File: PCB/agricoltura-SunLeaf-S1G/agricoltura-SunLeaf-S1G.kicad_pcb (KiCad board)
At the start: 4 copper layers, 100 x 40 mm, 125 parts, among them M1 SPSGRF-915, Q1 DMP3125L-7, Q2 DMP3125L-7, SW1 B3U-1000P, T1 BM04B-SRSS-TB(LF)(SN), T10 BM04B-SRSS-TB(LF)(SN), T11 BM04B-SRSS-TB(LF)(SN), T12 BM04B-SRSS-TB(LF)(SN), T13 BM04B-SRSS-TB(LF)(SN), T14 BM04B-SRSS-TB(LF)(SN), T15 BM04B-SRSS-TB(LF)(SN), T16 BM04B-SRSS-TB(LF)(SN), T17 BM04B-SRSS-TB(LF)(SN), T18 PPTC101LFBN-RC, T19 PPTC101LFBN-RC, T2 TC2050-IDC-NL-FP, T20 BU2032SM-JJ-GTR, T3 0475890001, T4 B2B-PH-K-S(LF)(SN), T5 B3B-PH-K-S(LF)(SN), T6 BM04B-SRSS-TB(LF)(SN), T7 BM04B-SRSS-TB(LF)(SN), T8 BM04B-SRSS-TB(LF)(SN), T9 BM04B-SRSS-TB(LF)(SN), U1 STM32F446RET6, U2 BQ24210DQCT, U3 AZ1117CR-3.3TRG1, U4 TCA9548APWR, U5 74HC4052D, U6 LTC2941CDCB-1#TRMPBF, X1 ABM3B-8.000MHZ-B2-T, X2 ABS07-32.768KHZ-9-T

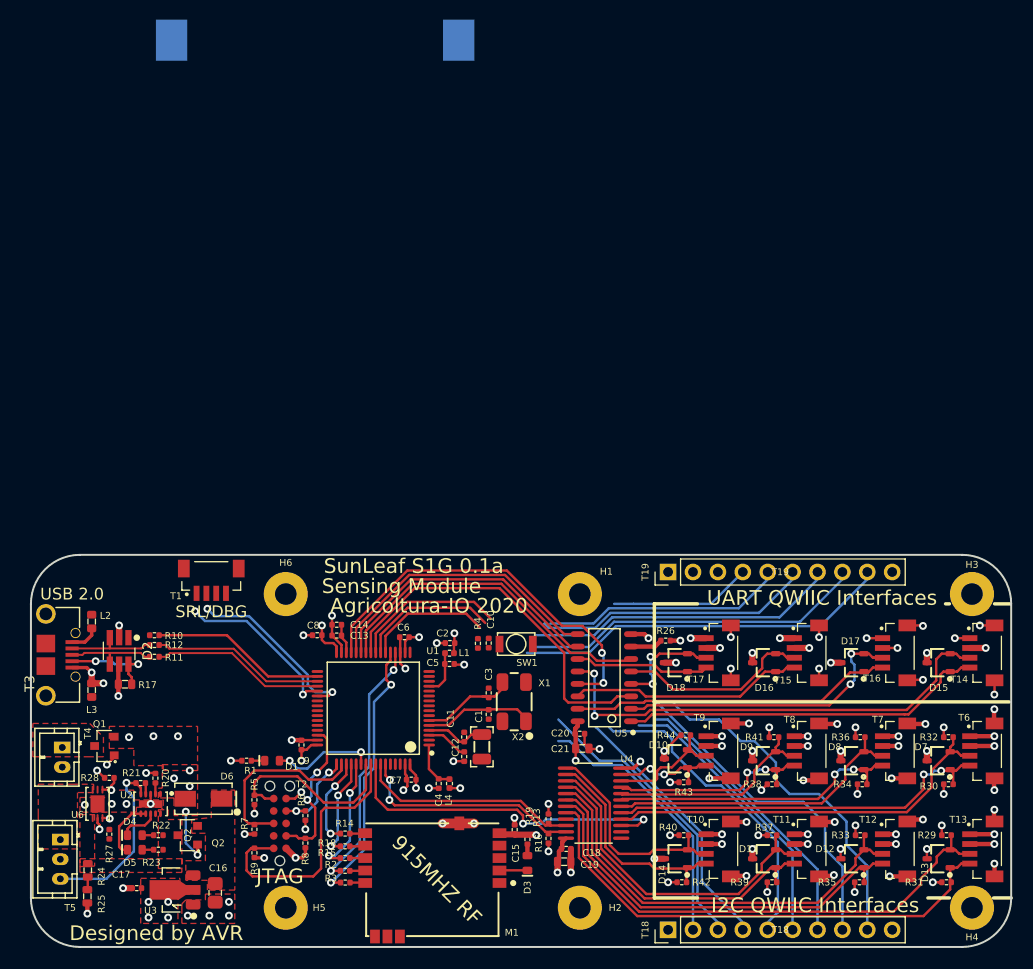
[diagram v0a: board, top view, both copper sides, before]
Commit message: Routing Complete
Board routing completed, also added EEPROM for storing configuration settings.
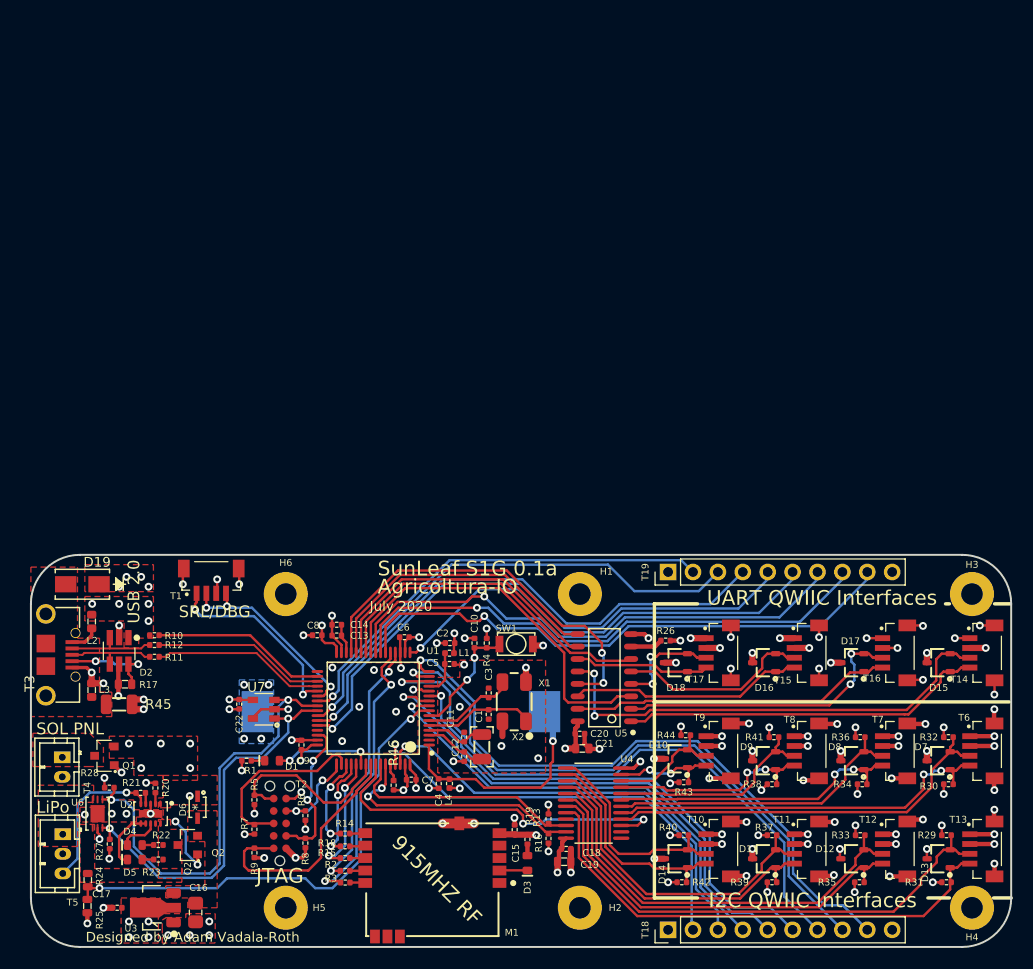
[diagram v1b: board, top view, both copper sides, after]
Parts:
- added C22: C0402C104K9PACTU, AVR-KiCAD-Lib-Resistors:R0402, F.Cu at (121.2, 85.2)
- added D19: SMAJ30CA, AVR-KiCAD-Lib-Diodes:SMAJ30CA, F.Cu at (105.2, 73.0)
- added R45: RC1206FR-071ML, AVR-KiCAD-Lib-Resistors:R1206, F.Cu at (109.0, 85.2)
- added R46: RC0402FR-071KL, AVR-KiCAD-Lib-Resistors:R0402, F.Cu at (137.0, 93.5)
- added U7: AT24C16D-STUM-T, AVR-KiCAD-Lib-ICs:SOT-23-5, F.Cu at (123.8, 85.8)
- D6: value B240A-13-F -> BAT20JFILM; footprint AVR-KiCAD-Lib-Diodes:B240A-13-F -> AVR-KiCAD-Lib-Diodes:BAT20JFILM
- moved T20 69.1 mm to (137.8, 86.0)
- moved C16 2.83 mm to (116.8, 106.5)
- moved C17 2.83 mm to (108.8, 106.0)
- moved U3 2.70 mm to (112.7, 106.0)
- moved C10 1.45 mm to (145.2, 79.0), turned to 90 degrees
- moved D6 1.06 mm to (117.0, 95.8), turned to 270 degrees
- moved R27 1.00 mm to (108.0, 99.5)
- moved D4 1.00 mm to (110.6, 99.6)
- moved D5 1.00 mm to (110.6, 101.1)
- moved Q1 1.00 mm to (107.5, 90.5)
- moved Q2 1.00 mm to (116.0, 99.6)
- moved R20 1.00 mm to (112.7, 93.8)
- moved R21 1.00 mm to (111.2, 94.3)
- moved R22 1.00 mm to (113.0, 99.6)
- moved R23 1.00 mm to (113.0, 101.1)
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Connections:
- T18 pad 2: Net-(T18-Pad2) -> /STM32F446RET6 - MCU/GPIO0
- T18 pad 3: Net-(T18-Pad3) -> /STM32F446RET6 - MCU/GPIO1
- T18 pad 4: Net-(T18-Pad4) -> /STM32F446RET6 - MCU/GPIO2
- T18 pad 5: Net-(T18-Pad5) -> /STM32F446RET6 - MCU/GPIO3
- T18 pad 6: Net-(T18-Pad6) -> /STM32F446RET6 - MCU/GPIO4
- T18 pad 7: Net-(T18-Pad7) -> /STM32F446RET6 - MCU/GPIO5
- T18 pad 8: Net-(T18-Pad8) -> /STM32F446RET6 - MCU/GPIO6
- T18 pad 9: Net-(T18-Pad9) -> /STM32F446RET6 - MCU/GPIO7
- T19 pad 2: Net-(T19-Pad2) -> /STM32F446RET6 - MCU/GPIO8
- T19 pad 3: Net-(T19-Pad3) -> /STM32F446RET6 - MCU/GPIO9
- T19 pad 4: Net-(T19-Pad4) -> /STM32F446RET6 - MCU/GPIO10
- T19 pad 5: Net-(T19-Pad5) -> /STM32F446RET6 - MCU/GPIO11
- T19 pad 6: Net-(T19-Pad6) -> /STM32F446RET6 - MCU/GPIO12
- T19 pad 7: Net-(T19-Pad7) -> /STM32F446RET6 - MCU/GPIO13
- T19 pad 8: Net-(T19-Pad8) -> /STM32F446RET6 - MCU/GPIO14
- T19 pad 9: Net-(T19-Pad9) -> /STM32F446RET6 - MCU/GPIO15
- U1 pad 10: Net-(U1-Pad10) -> /STM32F446RET6 - MCU/GPIO3
- U1 pad 11: Net-(U1-Pad11) -> /STM32F446RET6 - MCU/GPIO4
- U1 pad 14: Net-(U1-Pad14) -> /STM32F446RET6 - MCU/GPIO5
- U1 pad 15: Net-(U1-Pad15) -> /STM32F446RET6 - MCU/GPIO6
- U1 pad 16: Net-(U1-Pad16) -> /STM32F446RET6 - MCU/GPIO7
- U1 pad 17: Net-(U1-Pad17) -> /STM32F446RET6 - MCU/GPIO12
- U1 pad 22: Net-(U1-Pad22) -> /STM32F446RET6 - MCU/GPIO15
- U1 pad 23: Net-(U1-Pad23) -> /STM32F446RET6 - MCU/GPIO14
- U1 pad 24: Net-(U1-Pad24) -> /STM32F446RET6 - MCU/GPIO13
- U1 pad 39: Net-(U1-Pad39) -> /STM32F446RET6 - MCU/GPIO8
- U1 pad 40: Net-(U1-Pad40) -> /Power Supply & Battery Charging/BAT_SDA
- U1 pad 41: Net-(U1-Pad41) -> /Power Supply & Battery Charging/BAT_SCL
- U1 pad 42: Net-(U1-Pad42) -> /STM32F446RET6 - MCU/GPIO9
- U1 pad 43: Net-(U1-Pad43) -> /STM32F446RET6 - MCU/GPIO10
- U1 pad 44: Net-(U1-Pad44) -> /STM32F446RET6 - MCU/GPIO11
- U1 pad 61: Net-(U1-Pad61) -> /STM32F446RET6 - MCU/GPIO0
- U1 pad 62: Net-(U1-Pad62) -> /STM32F446RET6 - MCU/GPIO1
- U1 pad 9: Net-(U1-Pad9) -> /STM32F446RET6 - MCU/GPIO2
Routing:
- net /STM32F446RET6 - MCU/GPIO7: track 0.00 -> 65.4 mm, vias 0 -> 1
- net /STM32F446RET6 - MCU/GPIO5: track 0.00 -> 63.2 mm, vias 0 -> 1
- net /STM32F446RET6 - MCU/GPIO6: track 0.00 -> 63.0 mm, vias 0 -> 1
- net /STM32F446RET6 - MCU/GPIO11: track 0.00 -> 58.1 mm, vias 0 -> 1
- net /STM32F446RET6 - MCU/GPIO15: track 0.00 -> 56.9 mm, vias 0 -> 1
- net /STM32F446RET6 - MCU/GPIO10: track 0.00 -> 55.1 mm, vias 0 -> 1
- net /STM32F446RET6 - MCU/GPIO14: track 0.00 -> 54.6 mm, vias 0 -> 1
- net /STM32F446RET6 - MCU/GPIO13: track 0.00 -> 53.2 mm, vias 0 -> 1
- net /STM32F446RET6 - MCU/GPIO3: track 0.00 -> 53.0 mm, vias 0 -> 1
- net /STM32F446RET6 - MCU/GPIO4: track 0.00 -> 51.6 mm, vias 0 -> 1
- net /STM32F446RET6 - MCU/GPIO9: track 0.00 -> 50.5 mm, vias 0 -> 1
- net /Power Supply & Battery Charging/BAT_VOLT_SENSE: track 1.31 -> 50.3 mm, vias 0 -> 2
- net /STM32F446RET6 - MCU/GPIO2: track 0.00 -> 47.9 mm, vias 0 -> 1
- net /STM32F446RET6 - MCU/GPIO8: track 0.00 -> 45.9 mm, vias 0 -> 1
- net /STM32F446RET6 - MCU/GPIO12: track 0.00 -> 45.8 mm, vias 0 -> 1
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- added copper zone on B.Cu, net GND
- added copper zone on F.Cu, net Net-(D19-Pad2)
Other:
- board text added: "Agricoltura-IO"
- board text added: "July 2020"
- board text added: "LiPo"
- board text added: "RTC Backup Battery"
- board text added: "SOL PNL"
- board text removed: "Agricoltura-IO 2020"
- board text removed: "Designed by AVR"
- board text removed: "Sensing Module"

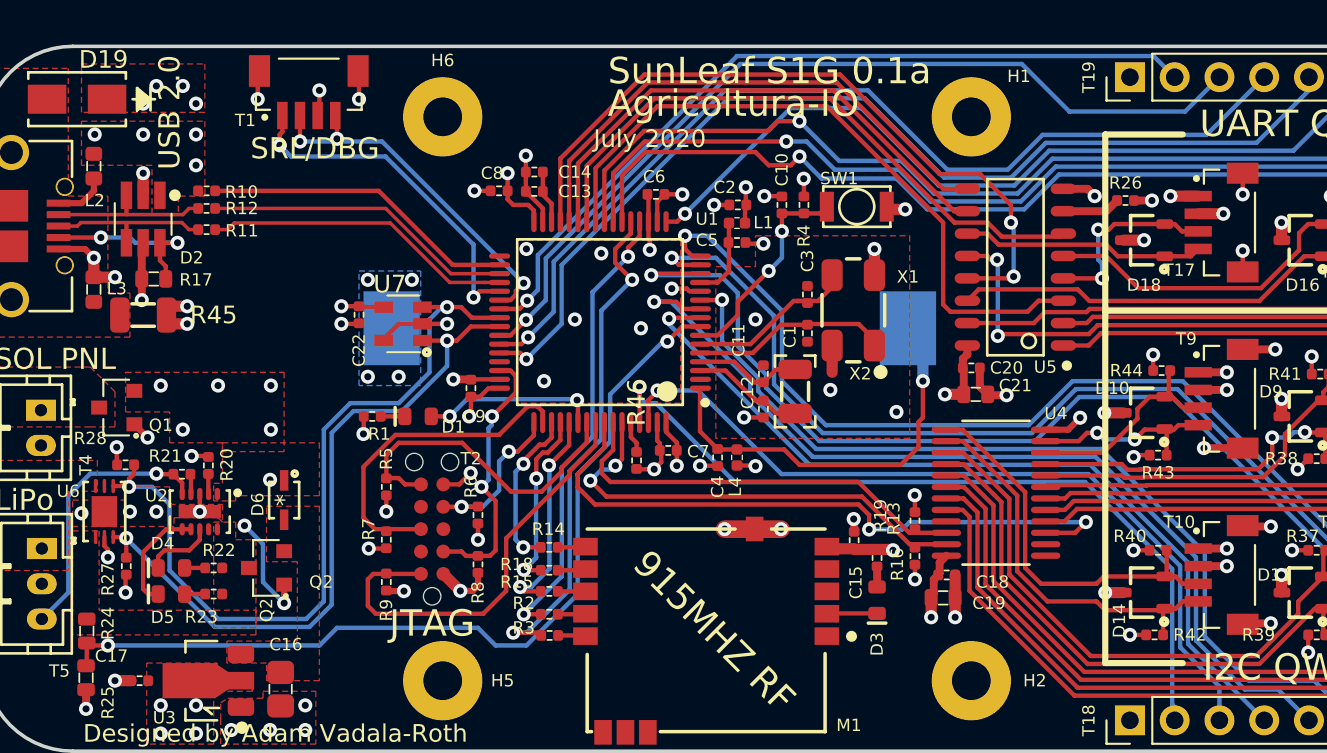
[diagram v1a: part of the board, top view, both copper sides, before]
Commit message: Adjusted Copper
Adjusted copper pours and via placement underneath MCU
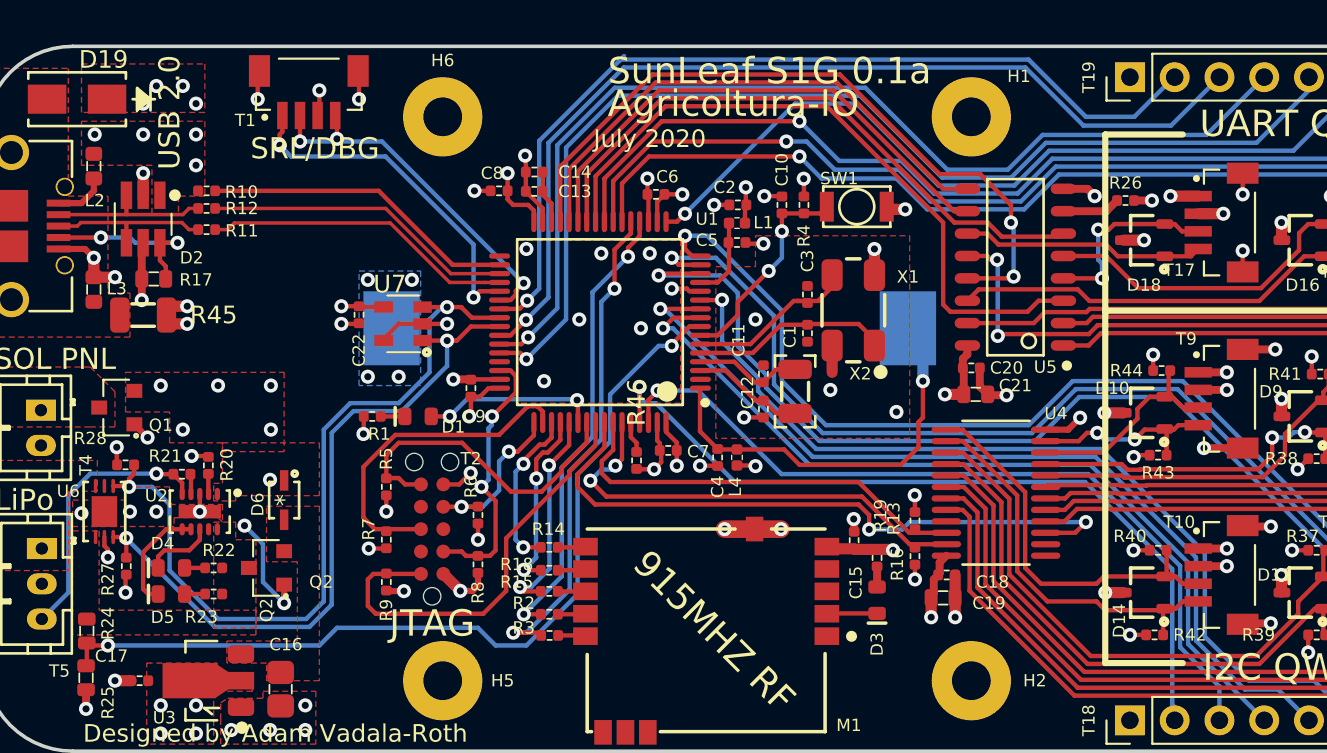
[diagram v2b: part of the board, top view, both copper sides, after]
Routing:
- net /STM32F446RET6 - MCU/GPIO8: track 45.9 -> 51.7 mm
- net /STM32F446RET6 - MCU/GPIO9: track 50.5 -> 54.8 mm
- net /STM32F446RET6 - MCU/GPIO11: track 58.1 -> 62.0 mm
- net /STM32F446RET6 - MCU/GPIO10: track 55.1 -> 58.9 mm
- net /STM32F446RET6 - MCU/GPIO3: track 53.0 -> 51.5 mm
- net /STM32F446RET6 - MCU/GPIO15: track 56.9 -> 56.0 mm
- net /STM32F446RET6 - MCU/GPIO5: track 63.2 -> 62.4 mm
- net /STM32F446RET6 - MCU/RF_SHDN_MCU: track 29.0 -> 28.2 mm
- net +3V3: track 113.7 -> 112.9 mm
- net /STM32F446RET6 - MCU/GPIO2: track 47.9 -> 48.4 mm
- net GND: vias 97 -> 98

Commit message: Pix
Pictures added
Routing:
- net /STM32F446RET6 - MCU/VBAT: track 23.3 -> 22.3 mm

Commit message: KiCAD 8
Projected updated to KiCAD 8
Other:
- net class Default removed
